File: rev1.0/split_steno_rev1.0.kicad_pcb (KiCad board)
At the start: 2 copper layers, 50 parts, among them J0 Audio-Jack-4, K0 KEYSW, K1 KEYSW, K10 KEYSW, K11 KEYSW, K12 KEYSW, K13 KEYSW, K14 KEYSW, K15 KEYSW, K16 KEYSW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

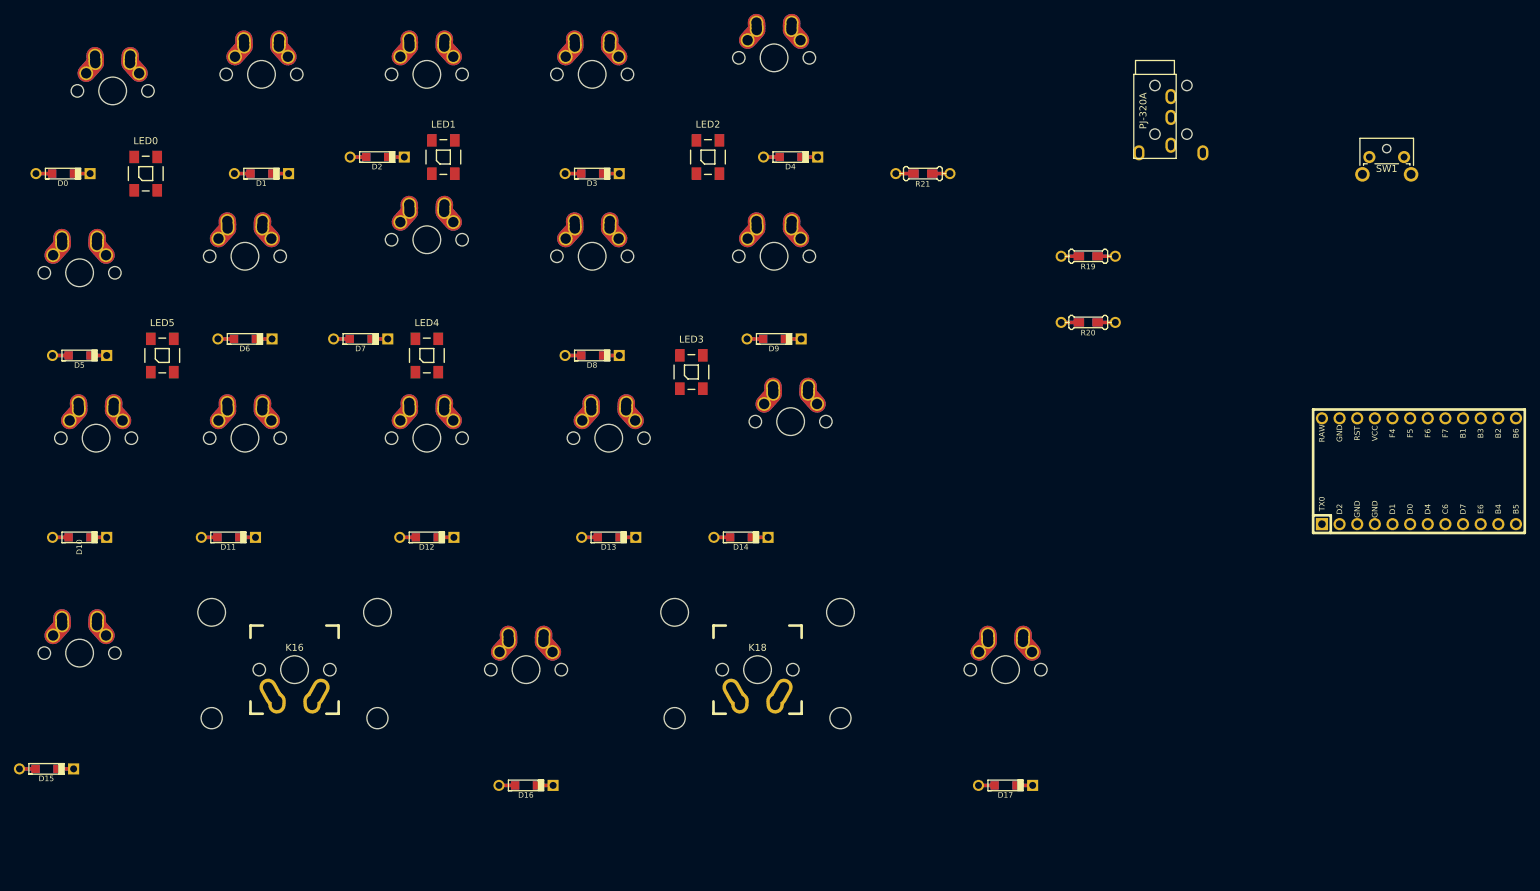
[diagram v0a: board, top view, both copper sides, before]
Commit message: laid out, added gnd plane
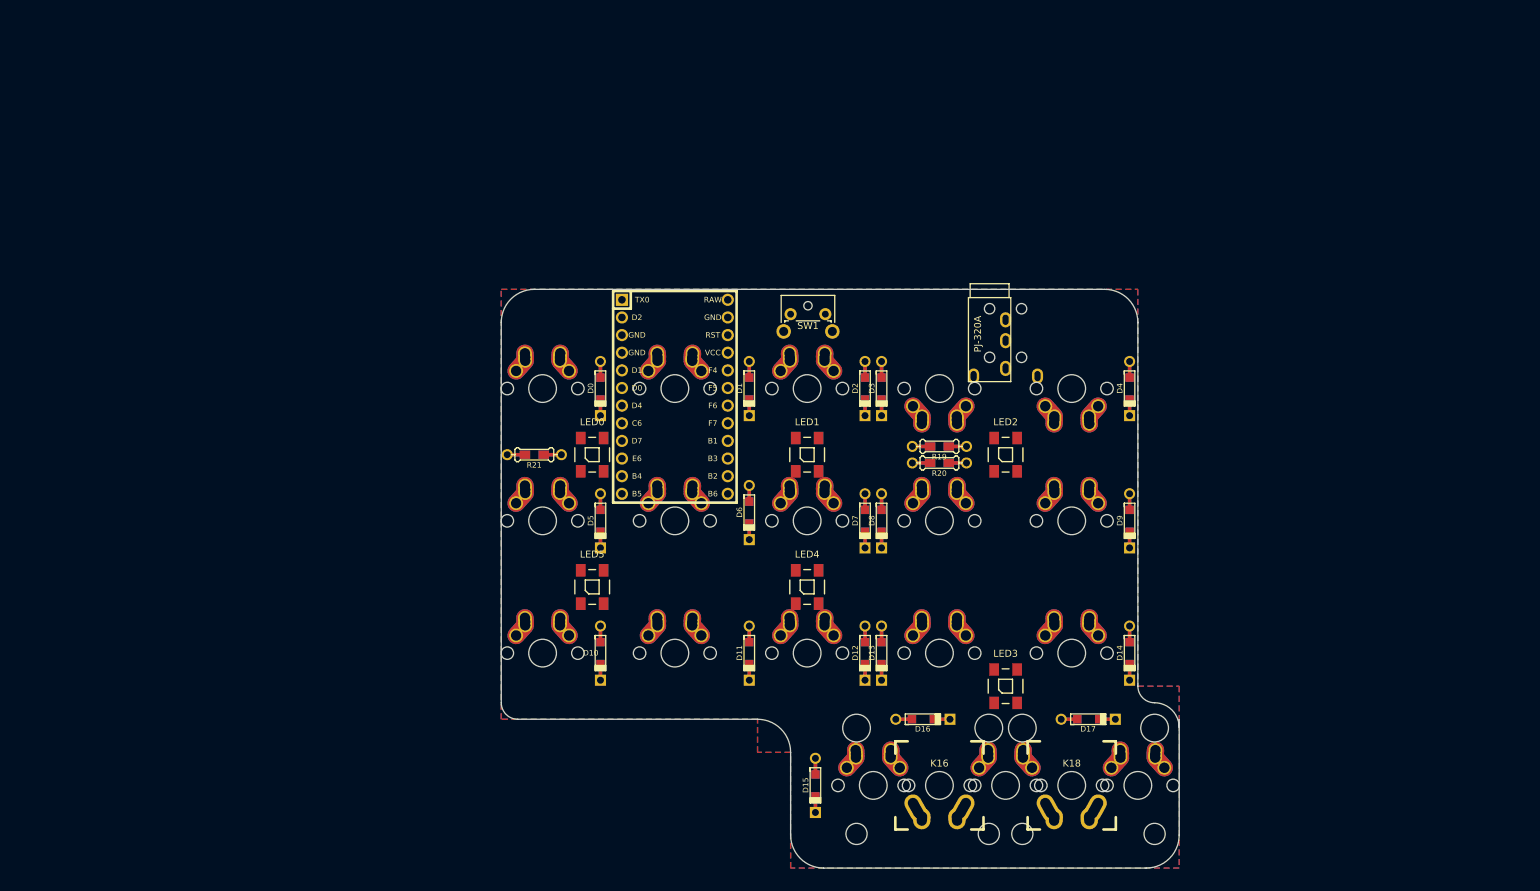
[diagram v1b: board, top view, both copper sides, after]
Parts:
- moved K15 115.9 mm to (154.8, 145.3)
- moved D15 110.8 mm to (146.4, 145.3), turned to 270 degrees
- moved U0 107.7 mm to (126.2, 89.3), turned to 270 degrees
- moved K16 94.4 mm to (164.3, 145.3)
- moved SW1 86.4 mm to (142.9, 77.4)
- moved D0 83.4 mm to (115.5, 88.1), turned to 270 degrees
- moved D5 78.7 mm to (115.5, 107.2), turned to 270 degrees
- moved D2 77.8 mm to (153.6, 88.1), turned to 270 degrees
- moved D7 77.2 mm to (153.6, 107.2), turned to 270 degrees
- moved D11 76.8 mm to (136.9, 126.2), turned to 270 degrees
- moved D10 76.8 mm to (115.5, 126.2), turned to 270 degrees
- moved D6 76.8 mm to (136.9, 106.0), turned to 270 degrees
- moved D1 76.8 mm to (136.9, 88.1), turned to 270 degrees
- moved LED0 76.0 mm to (114.3, 97.6)
- moved K5 75.6 mm to (107.2, 107.2)
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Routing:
- added copper zone on B.Cu, net GND
- added copper zone on F.Cu, net GND
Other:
- board outline added: 97.6 x 83.3 mm

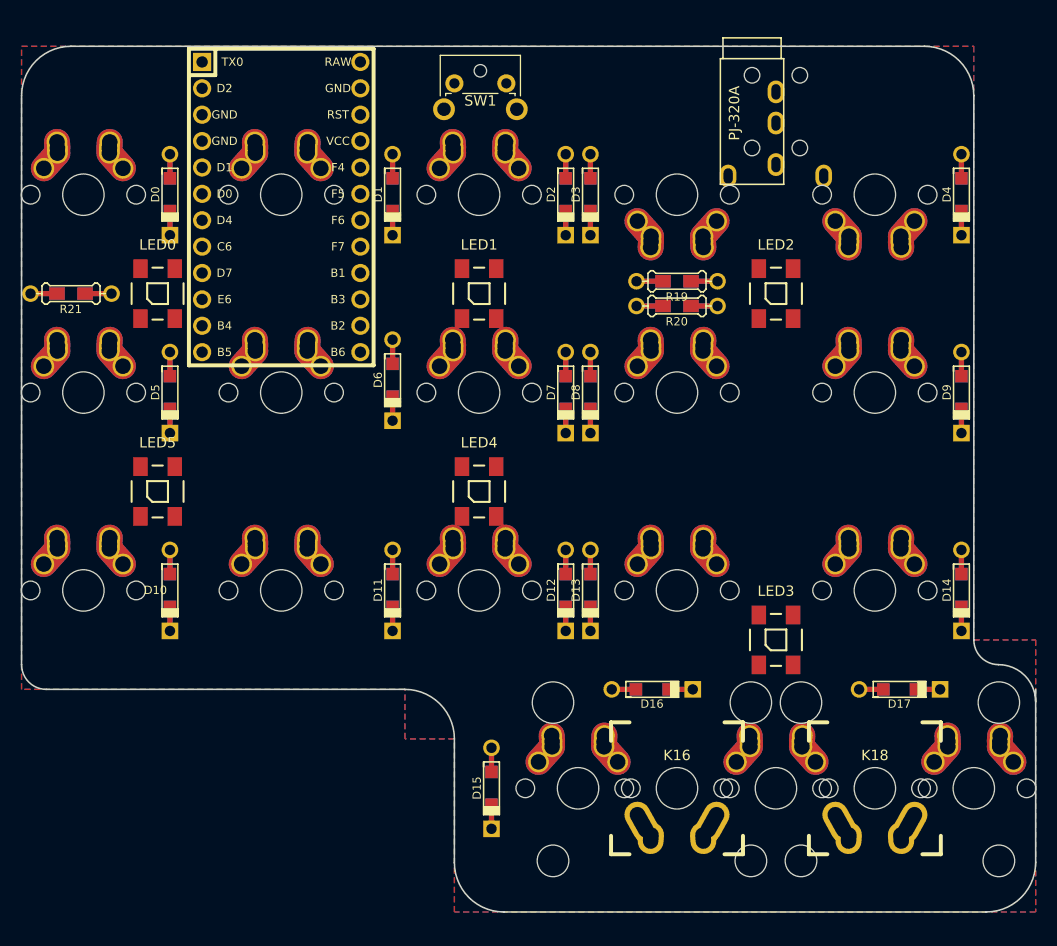
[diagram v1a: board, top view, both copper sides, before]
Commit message: removed ws2812b, replaced with breakout
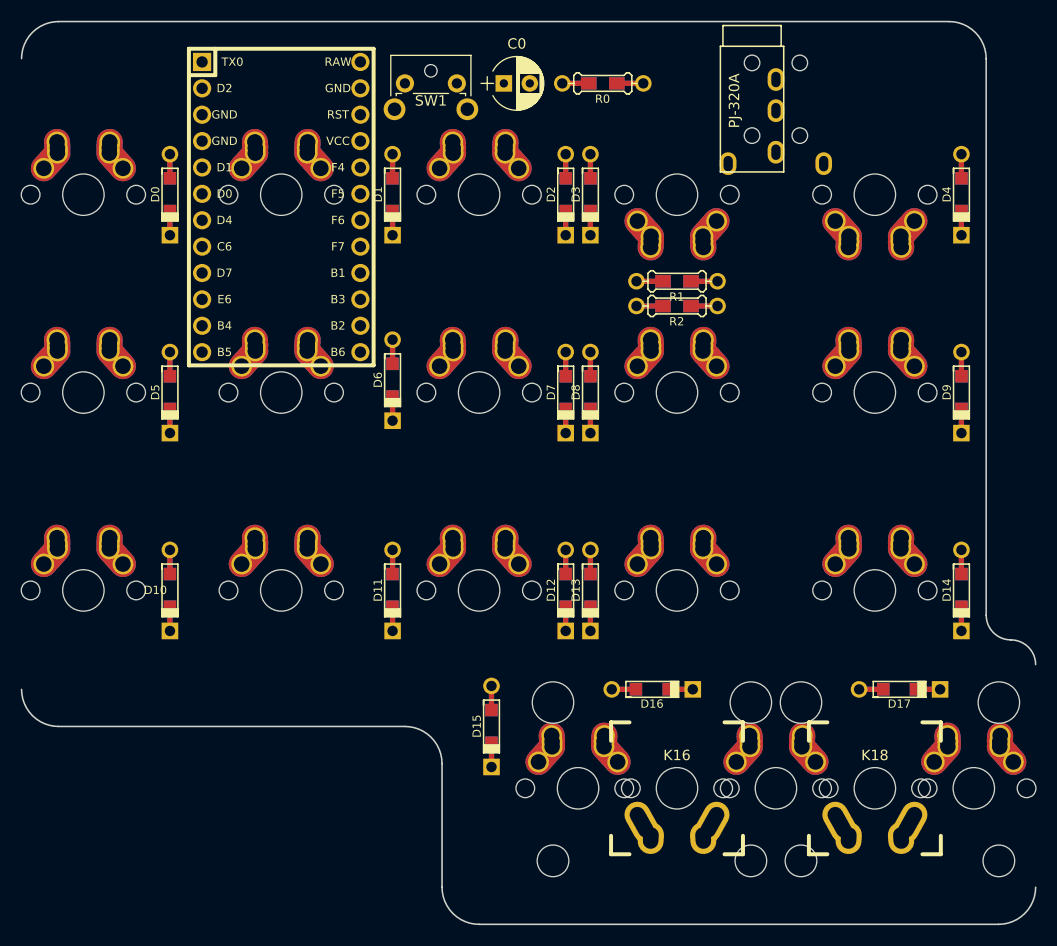
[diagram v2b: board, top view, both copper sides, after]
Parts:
- removed LED0, LED1, LED2, LED3, LED4, LED5: WS2812B, WS2812B:WS2812B
- removed R19, R20: 4.7k, Keebio-Parts:Resistor-Hybrid
- removed R21: 500, Keebio-Parts:Resistor-Hybrid
- added C0: CP, Capacitors_THT:CP_Radial_D5.0mm_P2.50mm, F.Cu at (147.6, 77.4)
- added R0: 500, Keebio-Parts:Resistor-Hybrid, F.Cu at (157.2, 77.4)
- added R1: 4.7k, Keebio-Parts:Resistor-Hybrid, F.Cu at (164.3, 96.4)
- added R2: 4.7k, Keebio-Parts:Resistor-Hybrid, F.Cu at (164.3, 98.8)
- moved D15 5.95 mm to (146.4, 139.3)
- moved SW1 4.76 mm to (138.1, 77.4)
- moved J0 1.19 mm to (173.8, 73.8)
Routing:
- removed copper zone on B.Cu, net GND
- removed copper zone on F.Cu, net GND
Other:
- board size 97.6 x 83.3 mm -> 97.6 x 86.9 mm

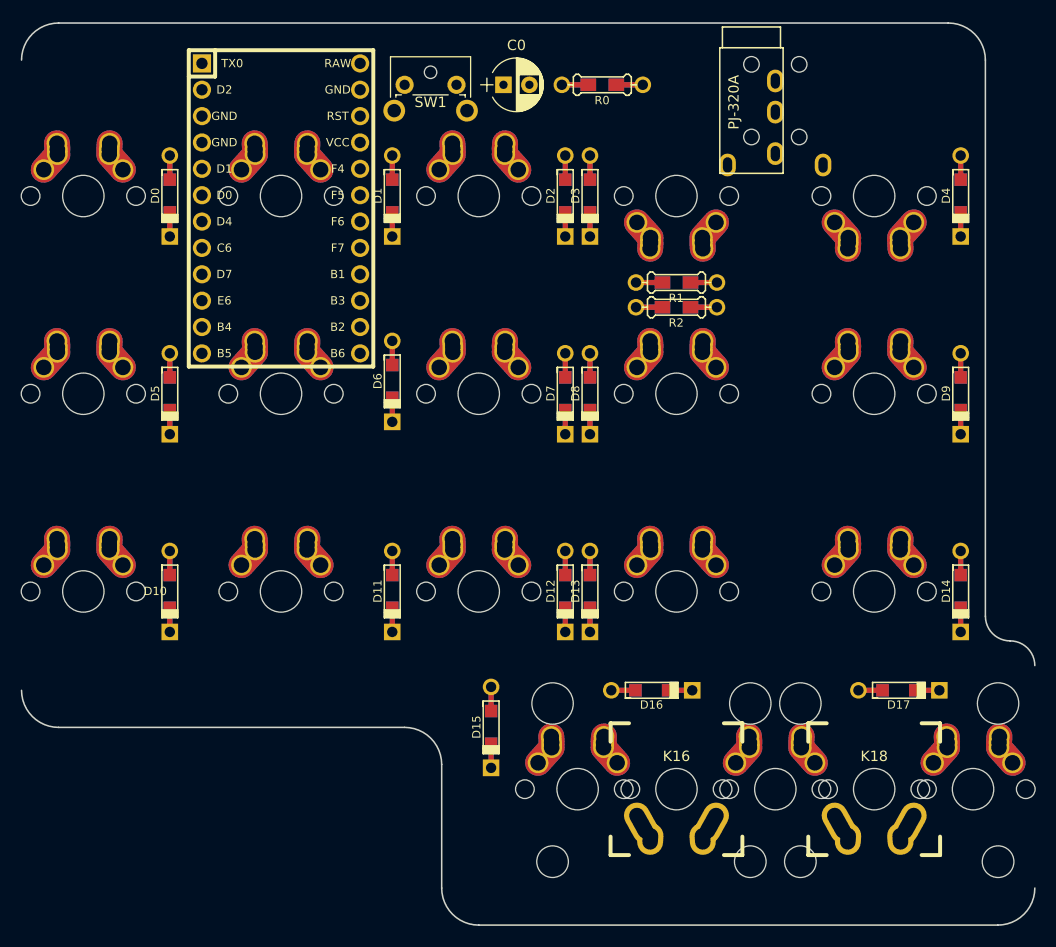
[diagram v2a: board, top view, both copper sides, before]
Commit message: route vcc
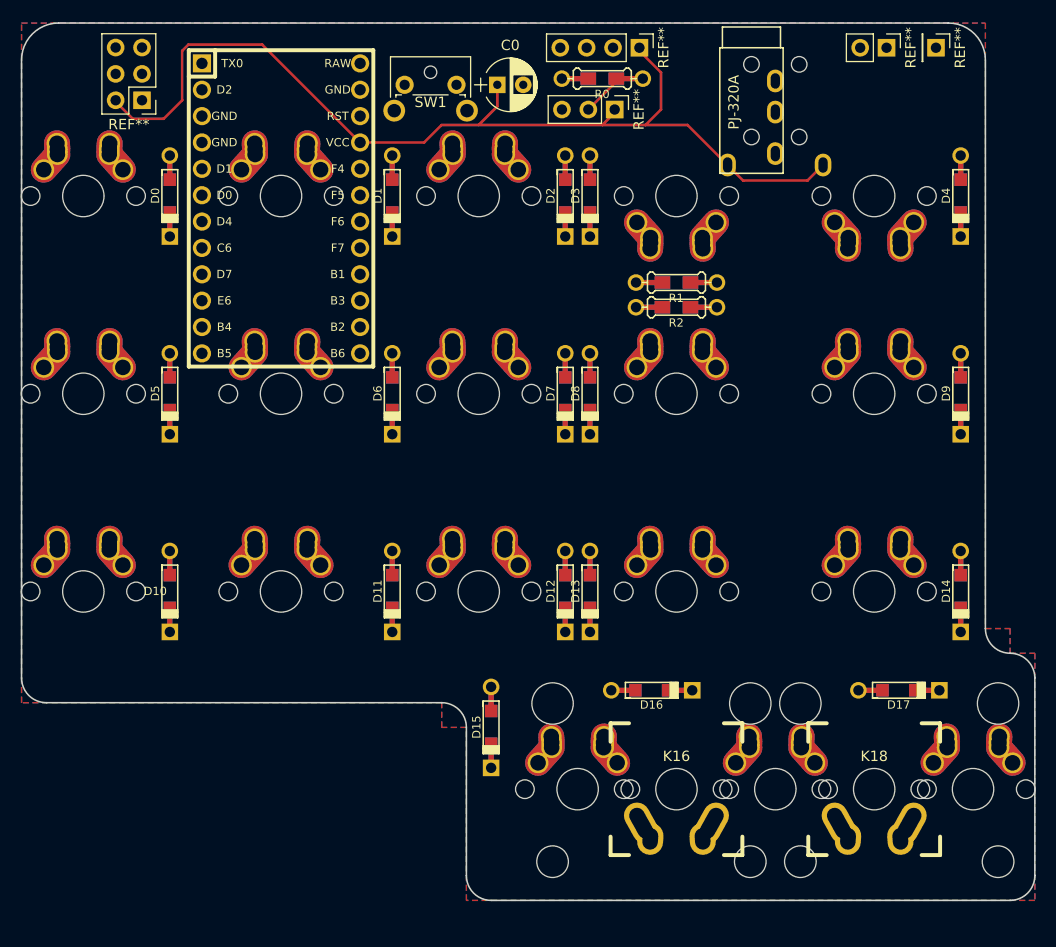
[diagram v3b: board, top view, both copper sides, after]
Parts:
- added REF**: ICSP, Pin_Headers:Pin_Header_Straight_2x03_Pitch2.54mm, F.Cu at (112.8, 78.9)
- added REF**: SERIAL, Pin_Headers:Pin_Header_Straight_1x04_Pitch2.54mm, F.Cu at (160.7, 73.8)
- added REF**: PWR, Pin_Headers:Pin_Header_Straight_1x02_Pitch2.54mm, F.Cu at (184.5, 73.8)
- added REF**: EXTRA, Pin_Headers:Pin_Header_Straight_1x01_Pitch2.54mm, F.Cu at (189.3, 73.8)
- added REF**: RGB, Pin_Headers:Pin_Header_Straight_1x03_Pitch2.54mm, F.Cu at (158.4, 79.8)
- moved D6 1.19 mm to (136.9, 107.2)
- moved R0 0.60 mm to (157.2, 76.8)
- moved C0 0.60 mm to (147.0, 77.4)
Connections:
- U0 pad 21: /row0 -> VCC
- U0 pad 23: (no net) -> GND
- U0 pad 3: /data1 -> GND
- U0 pad 4: /col0 -> GND
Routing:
- net VCC: track 0.00 -> 97.7 mm
- net /dout: track 0.00 -> 6.48 mm
- added copper zone on B.Cu, net GND
- added copper zone on F.Cu, net GND
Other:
- board size 97.6 x 86.9 mm -> 97.6 x 84.5 mm
